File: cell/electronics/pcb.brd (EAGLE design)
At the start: 49.6 x 49.9 mm, 27 parts, among them IC2 L293D, M1 M02PTH3, M2 M02PTH3, Q1 MOSFET-NCHANNEL2N7000, Q2 MOSFET-NCHANNEL2N7000, SW1 M02PTH3, SW2 M02PTH3, SW3 M02PTH3, SW4 M02PTH3, SW5 M02PTH3

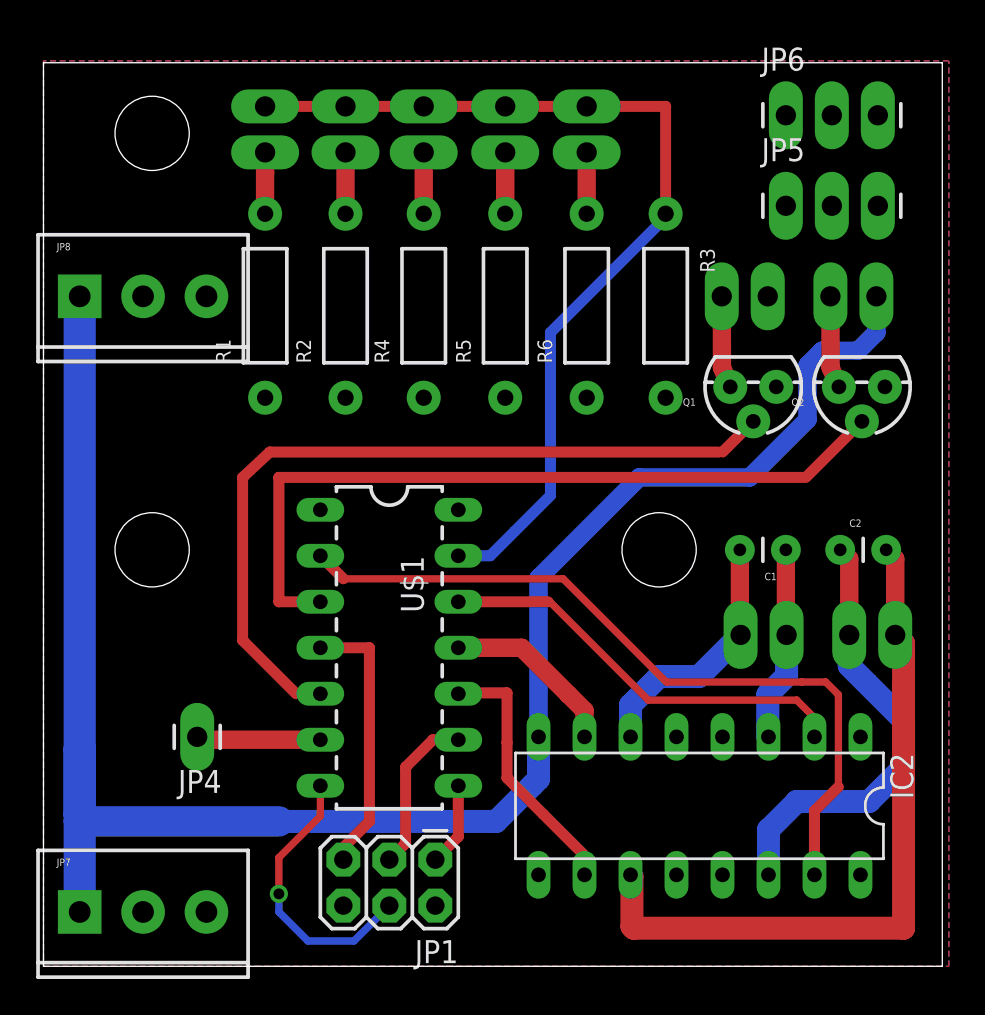
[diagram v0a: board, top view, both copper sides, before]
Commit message: Relaying out the board
laying out the board again for production, easier to read, components
aligned and placed better. ready for first rev production
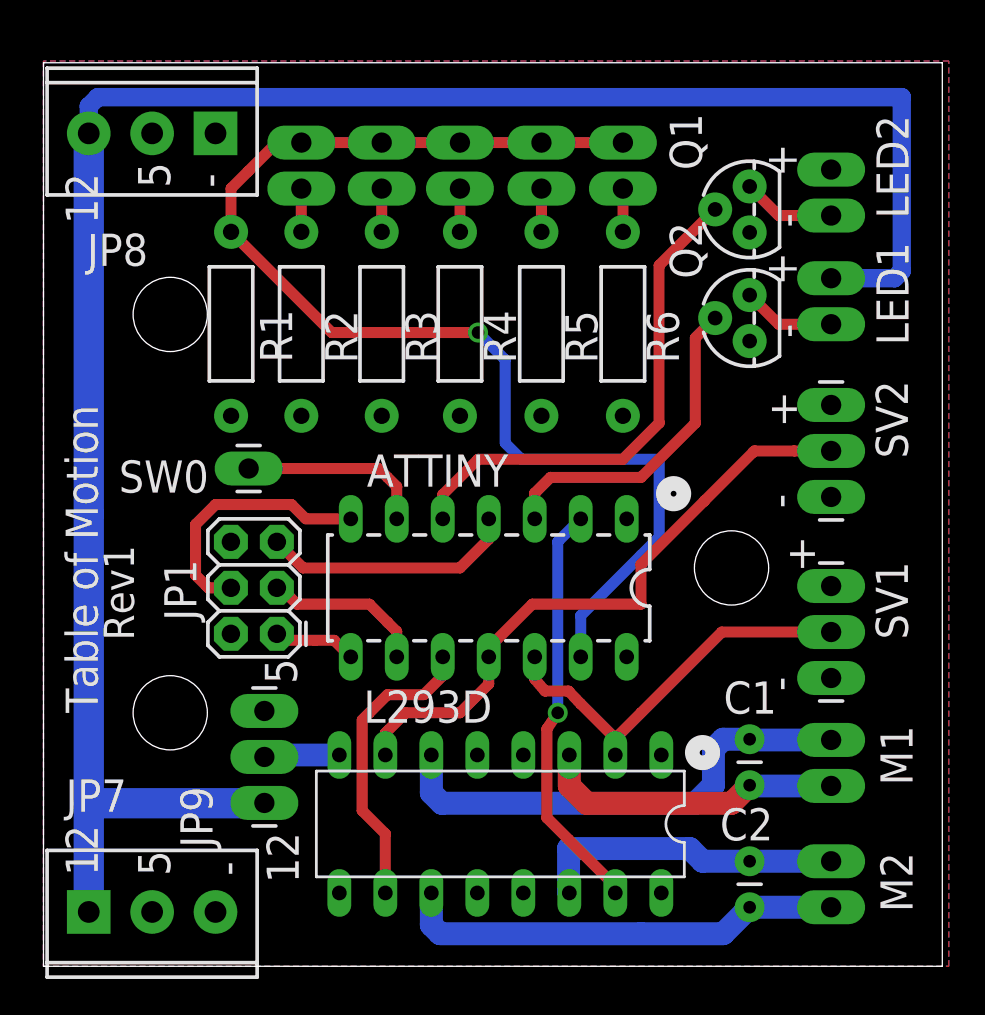
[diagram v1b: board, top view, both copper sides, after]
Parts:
- removed IC2: L293D, st-microelectronics:DIL16
- removed JP2, JP3: M02PTH3, SparkFun-Connectors:1X02_LONGPADS
- removed JP4: M01PTH_LONGPAD, SparkFun-Connectors:1X01_LONGPAD
- removed JP5, JP6: (no value), SparkFun-Connectors:1X03_LONGPADS
- removed U$1: ATTINY84ATTINY84-20PU, SparkFun-DigitalIC:DIL14
- added ATTINY: ATTINY84ATTINY84-20PU, SparkFun-DigitalIC:DIL14
- added JP9, SV1, SV2: (no value), SparkFun-Connectors:1X03_LONGPADS
- added L293D: L293D, st-microelectronics:DIL16
- added LED1, LED2: M02PTH3, SparkFun-Connectors:1X02_LONGPADS
- added SW0: M01PTH_LONGPAD, SparkFun-Connectors:1X01_LONGPAD
- moved C2 17.9 mm to (39.0, 5.80), turned to 270 degrees
- moved R3 15.7 mm to (18.7, 35.5), turned to 90 degrees
- moved JP1 15.2 mm to (12.9, 18.4), turned to 90 degrees
- moved C1 13.2 mm to (39.0, 10.0), turned to 90 degrees
- moved M2 12.5 mm to (43.5, 5.80), turned to 270 degrees
- moved JP8 11.7 mm to (9.50, 46.0), turned to 180 degrees
- moved Q1 9.80 mm to (39.0, 41.8), turned to 90 degrees
- moved M1 7.66 mm to (43.5, 12.5), turned to 270 degrees
- moved Q2 7.27 mm to (39.0, 35.8), turned to 90 degrees
- moved SW1 2.83 mm to (14.2, 45.5)
- moved SW2 2.83 mm to (18.7, 45.5)
- moved SW3 2.83 mm to (23.0, 45.5)
- moved SW4 2.83 mm to (27.5, 45.5)
- moved SW5 2.83 mm to (32.0, 45.5)
- moved R2 2.64 mm to (14.2, 35.5)
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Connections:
- new net N$17: JP9.2, L293D.8
- net 5V: now also ATTINY.1, JP9.1, L293D.1, L293D.16, L293D.9, LED2.1, R1.P$2, SV1.1, SV2.1; no longer IC2.1, IC2.16, IC2.9, JP3.1, JP5.1, JP6.1, R3.P$2, U$1.1
- net GND: now also ATTINY.14, JP8.1, L293D.12, L293D.13, L293D.4, L293D.5, R3.P$1, SV1.3, SV2.3; no longer IC2.12, IC2.13, IC2.4, IC2.5, JP5.3, JP6.3, JP8.3, R1.P$1, U$1.14
- net N$1: now also L293D.14; no longer IC2.14
- net N$10: now also ATTINY.13, R1.P$1; no longer R3.P$1, U$1.13
- net N$11: now also ATTINY.12, L293D.2, SV1.2; no longer IC2.2, JP6.2, U$1.12
- net N$12: now also R2.P$2; no longer R1.P$2
- net N$13: now also R3.P$2; no longer R2.P$2
- net N$14: now also ATTINY.7; no longer U$1.7
- net N$15: now also ATTINY.4; no longer U$1.4
- net N$16: now also ATTINY.8; no longer U$1.8
- net N$18: now also LED1.2; no longer JP2.2
- net N$19: now also LED2.2; no longer JP3.2
- net N$2: now also ATTINY.11, L293D.7, SV2.2; no longer IC2.7, JP5.2, U$1.11
- net N$20: now also ATTINY.3; no longer U$1.3
- net N$21: now also ATTINY.5; no longer U$1.5
- net N$3: now also ATTINY.6, SW0.1; no longer JP4.1, U$1.6
- net N$4: now also ATTINY.10, L293D.10; no longer IC2.10, U$1.10
- net N$5: now also L293D.11; no longer IC2.11
- net N$6: now also L293D.3; no longer IC2.3
- net N$7: now also L293D.6; no longer IC2.6
- net N$8: now also ATTINY.9; no longer U$1.9
- net N$9: now also ATTINY.2, L293D.15; no longer IC2.15, U$1.2
- net VCC: now also JP8.3, JP9.3, LED1.1; no longer IC2.8, JP2.1, JP8.1
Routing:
- net N$2: track 9.86 -> 34.7 mm
- net N$20: track 42.6 -> 18.1 mm
- net N$9: track 42.3 -> 22.9 mm, vias 0 -> 1
- net N$10: track 52.7 -> 69.3 mm, vias 0 -> 1
- net N$21: track 44.0 -> 28.0 mm
- net N$5: track 39.2 -> 24.7 mm
- net N$7: track 14.2 -> 27.1 mm
- net VCC: track 103.1 -> 113.0 mm
- net N$1: track 24.8 -> 17.3 mm
- net N$6: track 10.8 -> 17.0 mm
- net N$17: track 0.00 -> 4.37 mm
- net N$3: track 6.96 -> 10.4 mm
- net N$4: track 14.6 -> 16.6 mm
- net N$14: track 15.5 -> 14.4 mm, vias 1 -> 0
- net N$26: track 3.39 -> 2.39 mm
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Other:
- board text added: "+"
- board text added: "-"
- board text added: "12"
- board text added: "5"
- board text added: "LED1"
- board text added: "LED2"
- board text added: "M1"
- board text added: "M2"
- board text added: "Rev1"
- board text added: "Table of Motion"
